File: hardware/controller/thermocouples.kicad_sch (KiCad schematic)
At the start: 12 parts, among them J1 Conn_01x02_Pin, J2 Conn_01x02_Pin, J3 Conn_01x02_Pin, U2 MAX31855KASA, U3 MAX31855KASA, U4 MAX31855KASA

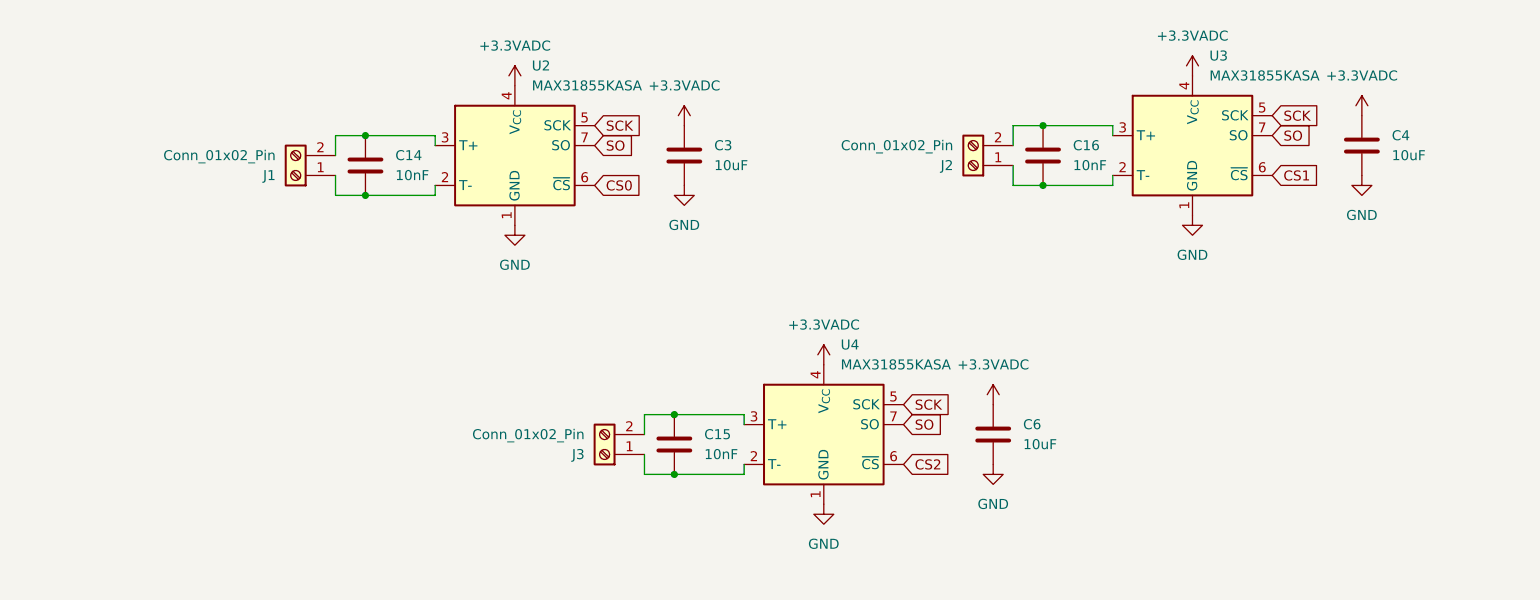
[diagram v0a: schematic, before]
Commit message: Add ferrites and more caps to thermocouples
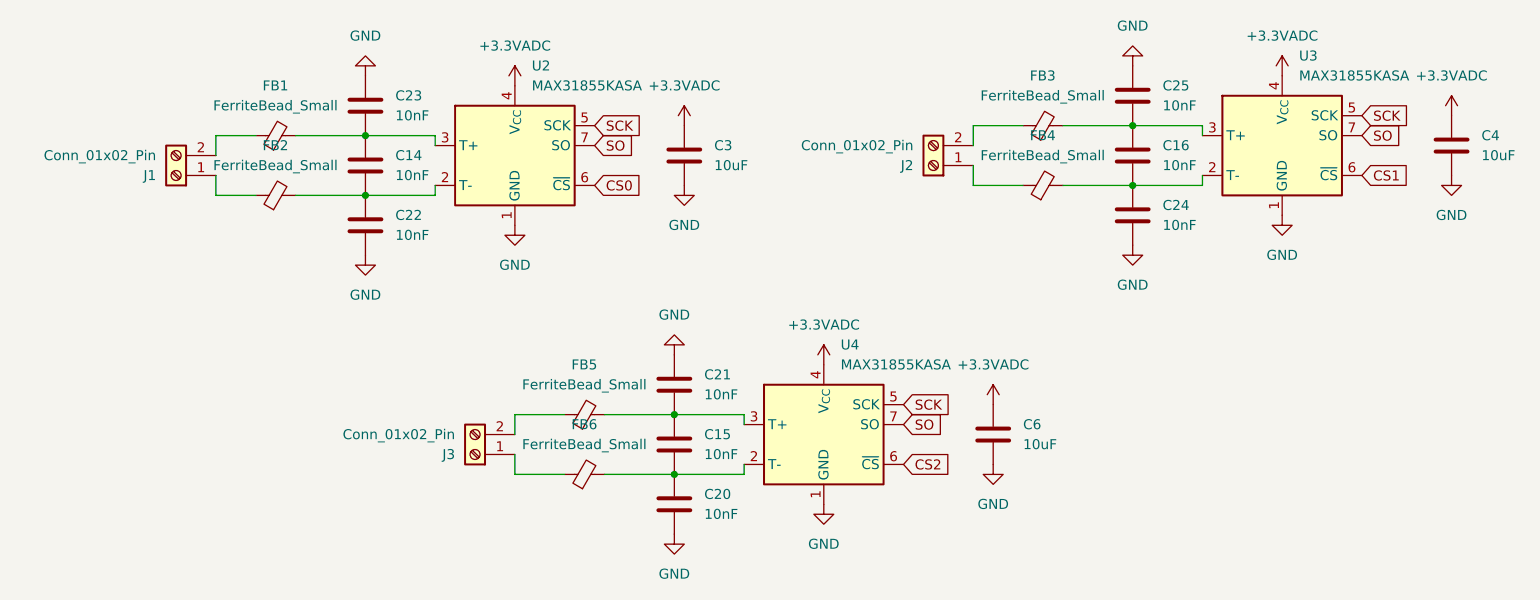
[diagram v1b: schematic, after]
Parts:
- added C20, C21, C22, C23, C24, C25: 10nF, Capacitor_SMD:C_0805_2012Metric, symbol Device:C
- added FB1, FB2, FB3, FB4, FB5, FB6: FerriteBead_Small, Capacitor_SMD:C_0805_2012Metric, symbol Device:FerriteBead_Small
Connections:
- net GND: now also C20.2, C21.1, C22.2, C23.1, C24.2, C25.1
- net at C15.2, U4.2 (T-): now also C20.1, FB6.2; no longer J3.1 (Pin_1)
- net at C15.1, U4.3 (T+): now also C21.2, FB5.2; no longer J3.2 (Pin_2)
- net at C16.2, U3.2 (T-): now also C24.1, FB4.2; no longer J2.1 (Pin_1)
- net at C16.1, U3.3 (T+): now also C25.2, FB3.2; no longer J2.2 (Pin_2)
- net at C14.1, U2.3 (T+): now also C23.2, FB1.2; no longer J1.2 (Pin_2)
- net at C14.2, U2.2 (T-): now also C22.1, FB2.2; no longer J1.1 (Pin_1)
- new net: FB6.1, J3.1 (Pin_1)
- new net: FB4.1, J2.1 (Pin_1)
- new net: FB3.1, J2.2 (Pin_2)
- new net: FB2.1, J1.1 (Pin_1)
- new net: FB1.1, J1.2 (Pin_2)
- new net: FB5.1, J3.2 (Pin_2)
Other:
- moved on the sheet: C16, C4, J1, J2, J3, U3
